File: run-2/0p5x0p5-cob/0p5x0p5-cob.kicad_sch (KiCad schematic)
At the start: 6 parts

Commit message: updating libs for 76 pin
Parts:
- U102: footprint WaferSpace:waferspace_p5xp5_padring -> WaferSpace:waferspace_p5xp5_padring_staggered
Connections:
- net GND: now also U102.58 (MP)
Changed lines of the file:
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@@
+	(wire
+		(pts
+			(xy 215.9 99.06) (xy 215.9 105.41)
+		)
+		(stroke
+			(width 0)
+			(type default)
+		)
+	)
 	(wire
 		(pts
@@
 				(path "/f44d2c8c-cc6e-4ce2-9d41-a48405cdfa9d"
 					(reference "#PWR030")
+					(unit 1)
+				)
+			)
+		)
+	)
+	(symbol
+		(lib_id "power:GND")
+		(at 215.9 105.41 0)
+		(unit 1)
+		(body_style 1)
+		(exclude_from_sim no)
+		(in_bom yes)
+		(on_board yes)
+		(in_pos_files yes)
+		(dnp no)
+		(fields_autoplaced yes)
+		(property "Reference" "#PWR010"
+			(at 215.9 111.76 0)
+			(hide yes)
+			(show_name no)
+			(do_not_autoplace no)
+			(effects
+				(font
+					(size 1.27 1.27)
+				)
+			)
+		)
+		(property "Value" "GND"
+			(at 215.9 110.49 0)
+			(show_name no)
+			(do_not_autoplace no)
+			(effects
+				(font
+					(size 1.27 1.27)
+				)
+			)
+		)
+		(property "Footprint" ""
+			(at 215.9 105.41 0)
+			(hide yes)
+			(show_name no)
+			(do_not_autoplace no)
+			(effects
+				(font
+					(size 1.27 1.27)
+				)
+			)
+		)
+		(property "Datasheet" ""
+			(at 215.9 105.41 0)
+			(hide yes)
+			(show_name no)
+			(do_not_autoplace no)
+			(effects
+				(font
+					(size 1.27 1.27)
+				)
+			)
+		)
+		(property "Description" "Power symbol creates a global label with name \"GND\" , ground"
+			(at 215.9 105.41 0)
+			(hide yes)
+			(show_name no)
+			(do_not_autoplace no)
+			(effects
+				(font
+					(size 1.27 1.27)
+				)
+			)
+		)
+		(pin "1"
+		)
+		(instances
+			(project "0p5x0p5-cob"
+				(path "/f44d2c8c-cc6e-4ce2-9d41-a48405cdfa9d"
+					(reference "#PWR010")
 					(unit 1)
 				)
@@
 			)
 		)
-		(property "Footprint" "WaferSpace:waferspace_p5xp5_padring"
+		(property "Footprint" "WaferSpace:waferspace_p5xp5_padring_staggered"
 			(at 179.07 99.06 0)
 			(hide yes)
@@
 		(pin "16"
 		)
+		(pin "58"
+		)
 		(instances

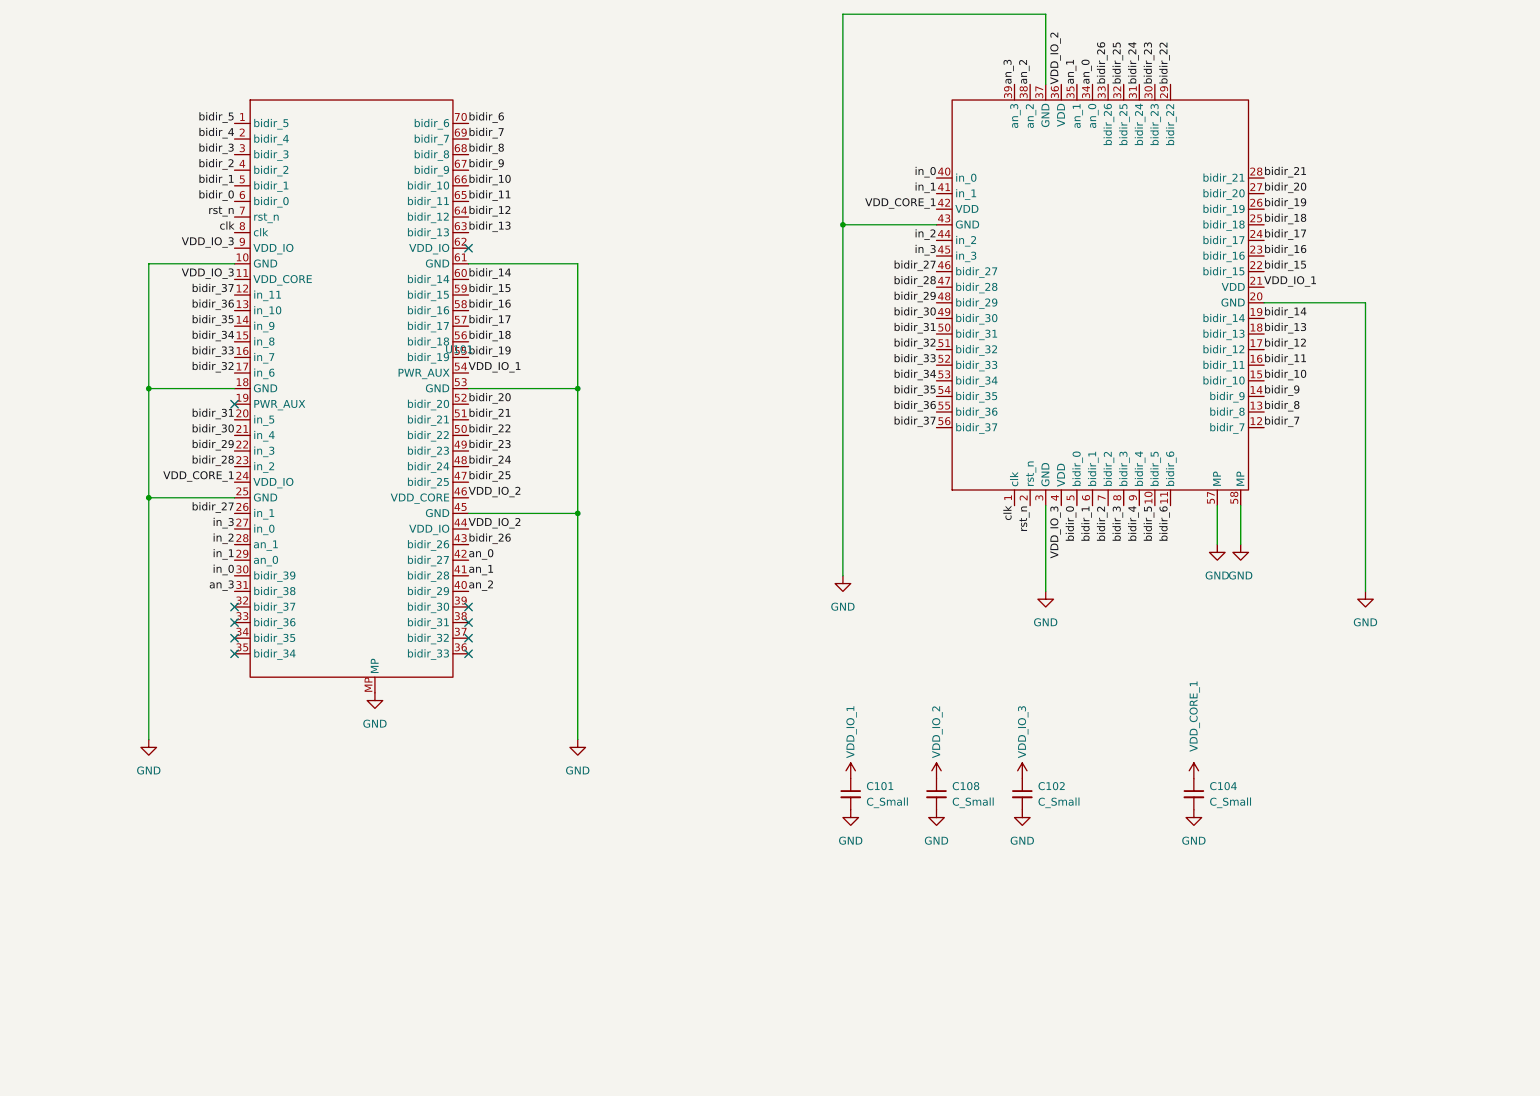
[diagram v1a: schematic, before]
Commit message: finished init routing front only
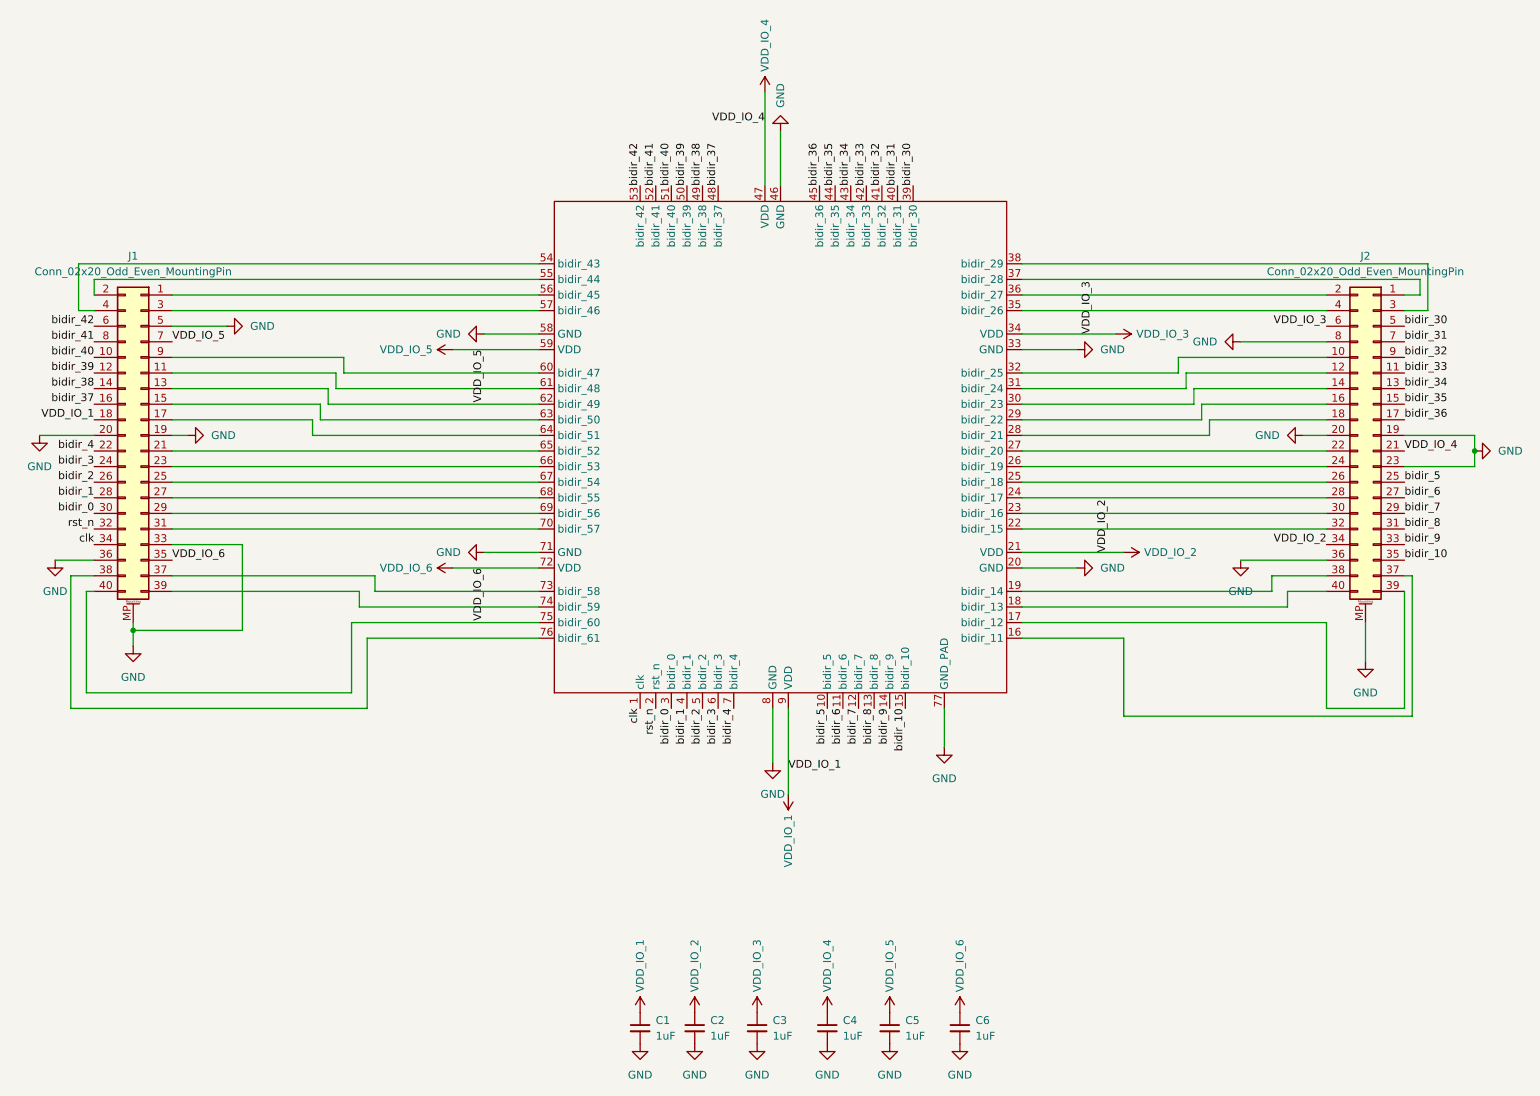
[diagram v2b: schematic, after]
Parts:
- removed C104: C_Small, Capacitor_SMD:C_0201_0603Metric, symbol Device:C_Small
- removed U101: (no value), WaferSpace:CONN-SMD_70P-P0.40_HCTL_HC-PBB40C-70DP-0.4V-02, symbol WaferSpace:70pin_ws_default_mezzanine
- removed U102: (no value), WaferSpace:waferspace_p5xp5_padring_staggered, symbol WaferSpace:0p5x0p5
- added C4, C5, C6: 1uF, Capacitor_SMD:C_0201_0603Metric, symbol Device:C_Small
- added J1, J2: Conn_02x20_Odd_Even_MountingPin, Connector_Hirose_DF40:Hirose_DF40C-40DP-0.4V_2x20-1MP_P0.4mm, symbol Connector_Generic_MountingPin:Conn_02x20_Odd_Even_MountingPin
- added U1: (no value), WaferSpace:0p5x0p5_76, symbol WaferSpace:0p5x0p5_76
- C1: renamed from C101; value C_Small -> 1uF
- C2: renamed from C108; value C_Small -> 1uF
- C3: renamed from C102; value C_Small -> 1uF
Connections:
- net GND: now also C4.2, C5.2, C6.2, J1.19 (Pin_19), J1.20 (Pin_20), J1.33 (Pin_33), J1.36 (Pin_36), J1.5 (Pin_5), J1.MP (MountPin), J2.19 (Pin_19), J2.20 (Pin_20), J2.23 (Pin_23), J2.36 (Pin_36), J2.8 (Pin_8), J2.MP (MountPin), U1.20 (GND), U1.33 (GND), U1.46 (GND), U1.58 (GND), U1.71 (GND), U1.77 (GND_PAD), U1.8 (GND)
- net VDD_IO_1: now also J1.18 (Pin_18), U1.9 (VDD)
- net VDD_IO_2: now also J2.34 (Pin_34), U1.21 (VDD)
- net VDD_IO_3: now also J2.6 (Pin_6), U1.34 (VDD)
- net bidir_0: now also J1.30 (Pin_30), U1.3 (bidir_0)
- net bidir_1: now also J1.28 (Pin_28), U1.4 (bidir_1)
- net bidir_10: now also J2.35 (Pin_35), U1.15 (bidir_10)
- net bidir_2: now also J1.26 (Pin_26), U1.5 (bidir_2)
- net bidir_3: now also J1.24 (Pin_24), U1.6 (bidir_3)
- net bidir_30: now also J2.5 (Pin_5), U1.39 (bidir_30)
- net bidir_31: now also J2.7 (Pin_7), U1.40 (bidir_31)
- net bidir_32: now also J2.9 (Pin_9), U1.41 (bidir_32)
- net bidir_33: now also J2.11 (Pin_11), U1.42 (bidir_33)
- net bidir_34: now also J2.13 (Pin_13), U1.43 (bidir_34)
- net bidir_35: now also J2.15 (Pin_15), U1.44 (bidir_35)
- net bidir_36: now also J2.17 (Pin_17), U1.45 (bidir_36)
- net bidir_37: now also J1.16 (Pin_16), U1.48 (bidir_37)
- net bidir_4: now also J1.22 (Pin_22), U1.7 (bidir_4)
- net bidir_5: now also J2.25 (Pin_25), U1.10 (bidir_5)
- net bidir_6: now also J2.27 (Pin_27), U1.11 (bidir_6)
- net bidir_7: now also J2.29 (Pin_29), U1.12 (bidir_7)
- net bidir_8: now also J2.31 (Pin_31), U1.13 (bidir_8)
- net bidir_9: now also J2.33 (Pin_33), U1.14 (bidir_9)
- net clk: now also J1.34 (Pin_34), U1.1 (clk)
- net rst_n: now also J1.32 (Pin_32), U1.2 (rst_n)
- new net: J2.1 (Pin_1), U1.37 (bidir_28)
- new net: J2.10 (Pin_10), U1.32 (bidir_25)
- new net: J2.12 (Pin_12), U1.31 (bidir_24)
- new net: J2.14 (Pin_14), U1.30 (bidir_23)
- new net: J2.16 (Pin_16), U1.29 (bidir_22)
- new net: J2.18 (Pin_18), U1.28 (bidir_21)
- new net: J2.2 (Pin_2), U1.36 (bidir_27)
- new net: J2.22 (Pin_22), U1.27 (bidir_20)
- new net: J2.24 (Pin_24), U1.26 (bidir_19)
- new net: J2.26 (Pin_26), U1.25 (bidir_18)
- new net: J2.28 (Pin_28), U1.24 (bidir_17)
- new net: J2.3 (Pin_3), U1.38 (bidir_29)
- new net: J2.30 (Pin_30), U1.23 (bidir_16)
- new net: J2.32 (Pin_32), U1.22 (bidir_15)
- new net: J2.37 (Pin_37), U1.16 (bidir_11)
- new net: J2.38 (Pin_38), U1.19 (bidir_14)
- new net: J2.39 (Pin_39), U1.17 (bidir_12)
- new net: J2.4 (Pin_4), U1.35 (bidir_26)
- new net: J2.40 (Pin_40), U1.18 (bidir_13)
- new net: J1.1 (Pin_1), U1.56 (bidir_45)
- new net: J1.11 (Pin_11), U1.61 (bidir_48)
- new net: J1.13 (Pin_13), U1.62 (bidir_49)
- new net: J1.15 (Pin_15), U1.63 (bidir_50)
- new net: J1.17 (Pin_17), U1.64 (bidir_51)
- new net: J1.2 (Pin_2), U1.55 (bidir_44)
- new net: J1.21 (Pin_21), U1.65 (bidir_52)
- new net: J1.23 (Pin_23), U1.66 (bidir_53)
- new net: J1.25 (Pin_25), U1.67 (bidir_54)
- new net: J1.27 (Pin_27), U1.68 (bidir_55)
- new net: J1.29 (Pin_29), U1.69 (bidir_56)
- new net: J1.3 (Pin_3), U1.57 (bidir_46)
- new net: J1.31 (Pin_31), U1.70 (bidir_57)
- new net: J1.37 (Pin_37), U1.73 (bidir_58)
- new net: J1.38 (Pin_38), U1.76 (bidir_61)
- new net: J1.39 (Pin_39), U1., U1.74 (bidir_59)
- new net: J1.4 (Pin_4), U1.54 (bidir_43)
- new net: J1.40 (Pin_40), U1.75 (bidir_60)
- new net: J1.9 (Pin_9), U1.60 (bidir_47)
- new net VDD_IO_4: C4.1, J2.21 (Pin_21), U1.47 (VDD)
- new net VDD_IO_5: C5.1, J1.7 (Pin_7), U1.59 (VDD)
- new net VDD_IO_6: C6.1, J1.35 (Pin_35), U1.72 (VDD)
- new net bidir_38: J1.14 (Pin_14), U1.49 (bidir_38)
- new net bidir_39: J1.12 (Pin_12), U1.50 (bidir_39)
- new net bidir_40: J1.10 (Pin_10), U1.51 (bidir_40)
- new net bidir_41: J1.8 (Pin_8), U1.52 (bidir_41)
- new net bidir_42: J1.6 (Pin_6), U1.53 (bidir_42)
- no-connect marks 10 -> 0
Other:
- moved on the sheet: C1, C2, C3

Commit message: designed v1 of 76 pin package
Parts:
- added CAT_1: pusheen_graphics, WaferSpace:pusheen_back, symbol Connector:Conn_01x01_Pin
- U1: footprint WaferSpace:0p5x0p5_76 -> WaferSpace:waferspace_p5xp5_padring_staggered
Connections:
- net GND: now also U1.78 (GND_PAD), U1.79 (GND_PAD), U1.80 (GND_PAD), U1.81 (GND_PAD)
- net at J2.37 (Pin_37): now also U1.17 (bidir_12); no longer U1.16 (bidir_11)
- net at J2.39 (Pin_39): now also U1.16 (bidir_11); no longer U1.17 (bidir_12)
- net at J1.38 (Pin_38): now also U1.75 (bidir_60); no longer U1.76 (bidir_61)
- net at J1.40 (Pin_40): now also U1.76 (bidir_61); no longer U1.75 (bidir_60)
- no-connect marks 0 -> 1
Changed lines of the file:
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@@
 	)
 	(junction
+		(at 172.72 134.62)
+		(diameter 0)
+		(color 0 0 0 0)
+	)
+	(junction
+		(at 170.18 134.62)
+		(diameter 0)
+		(color 0 0 0 0)
+	)
+	(junction
+		(at 167.64 134.62)
+		(diameter 0)
+		(color 0 0 0 0)
+	)
+	(junction
 		(at 254 90.17)
 		(diameter 0)
 		(color 0 0 0 0)
 	)
+	(junction
+		(at 175.26 134.62)
+		(diameter 0)
+		(color 0 0 0 0)
+	)
+	(no_connect
+		(at 49.53 176.53)
+	)
 	(wire
 		(pts
@@
 	(wire
 		(pts
-			(xy 27.94 129.54) (xy 71.12 129.54)
+			(xy 69.85 77.47) (xy 101.6 77.47)
 		)
 		(stroke
@@
 	(wire
 		(pts
-			(xy 69.85 77.47) (xy 101.6 77.47)
+			(xy 139.7 132.08) (xy 139.7 140.97)
 		)
 		(stroke
@@
 	(wire
 		(pts
-			(xy 139.7 132.08) (xy 139.7 140.97)
+			(xy 180.34 95.25) (xy 229.87 95.25)
 		)
 		(stroke
@@
 	(wire
 		(pts
-			(xy 180.34 95.25) (xy 229.87 95.25)
+			(xy 180.34 71.12) (xy 195.58 71.12)
 		)
 		(stroke
@@
 	(wire
 		(pts
-			(xy 180.34 71.12) (xy 195.58 71.12)
+			(xy 207.01 80.01) (xy 207.01 77.47)
 		)
 		(stroke
@@
 	(wire
 		(pts
-			(xy 207.01 80.01) (xy 207.01 77.47)
+			(xy 41.91 92.71) (xy 101.6 92.71)
 		)
 		(stroke
@@
 	(wire
 		(pts
-			(xy 41.91 92.71) (xy 101.6 92.71)
+			(xy 229.87 132.08) (xy 247.65 132.08)
 		)
 		(stroke
@@
 	(wire
 		(pts
+			(xy 27.94 132.08) (xy 73.66 132.08)
+		)
+		(stroke
+			(width 0)
+			(type default)
+		)
+	)
+	(wire
+		(pts
 			(xy 207.01 77.47) (xy 229.87 77.47)
 		)
@@
 	(wire
 		(pts
+			(xy 177.8 134.62) (xy 175.26 134.62)
+		)
+		(stroke
+			(width 0)
+			(type default)
+		)
+	)
+	(wire
+		(pts
 			(xy 41.91 85.09) (xy 64.77 85.09)
 		)
@@
 	(wire
 		(pts
+			(xy 242.57 133.35) (xy 196.85 133.35)
+		)
+		(stroke
+			(width 0)
+			(type default)
+		)
+	)
+	(wire
+		(pts
 			(xy 67.31 80.01) (xy 67.31 82.55)
 		)
@@
 	(wire
 		(pts
+			(xy 177.8 132.08) (xy 177.8 134.62)
+		)
+		(stroke
+			(width 0)
+			(type default)
+		)
+	)
+	(wire
+		(pts
 			(xy 68.58 80.01) (xy 101.6 80.01)
 		)
@@
 	(wire
 		(pts
-			(xy 243.84 110.49) (xy 243.84 133.35)
+			(xy 175.26 132.08) (xy 175.26 134.62)
 		)
 		(stroke
@@
 	(wire
 		(pts
-			(xy 243.84 133.35) (xy 196.85 133.35)
+			(xy 210.82 87.63) (xy 210.82 85.09)
 		)
 		(stroke
@@
 	(wire
 		(pts
-			(xy 210.82 87.63) (xy 210.82 85.09)
+			(xy 41.91 95.25) (xy 101.6 95.25)
 		)
 		(stroke
@@
 	(wire
 		(pts
-			(xy 41.91 95.25) (xy 101.6 95.25)
+			(xy 246.38 59.69) (xy 246.38 67.31)
 		)
 		(stroke
@@
 	(wire
 		(pts
-			(xy 246.38 59.69) (xy 246.38 67.31)
+			(xy 25.4 129.54) (xy 71.12 129.54)
 		)
 		(stroke
@@
 	(wire
 		(pts
+			(xy 167.64 134.62) (xy 170.18 134.62)
+		)
+		(stroke
+			(width 0)
+			(type default)
+		)
+	)
+	(wire
+		(pts
 			(xy 41.91 113.03) (xy 72.39 113.03)
 		)
@@
 	(wire
 		(pts
-			(xy 167.64 132.08) (xy 167.64 138.43)
+			(xy 167.64 132.08) (xy 167.64 134.62)
 		)
 		(stroke
@@
 	(wire
 		(pts
-			(xy 242.57 132.08) (xy 242.57 113.03)
+			(xy 41.91 82.55) (xy 66.04 82.55)
 		)
 		(stroke
@@
 	(wire
 		(pts
-			(xy 41.91 82.55) (xy 66.04 82.55)
+			(xy 175.26 134.62) (xy 172.72 134.62)
 		)
 		(stroke
@@
 	(wire
 		(pts
-			(xy 27.94 113.03) (xy 27.94 129.54)
-		)
-		(stroke
-			(width 0)
-			(type default)
-		)
-	)
-	(wire
-		(pts
 			(xy 87.63 109.22) (xy 101.6 109.22)
 		)
@@
 	(wire
 		(pts
-			(xy 25.4 132.08) (xy 73.66 132.08)
+			(xy 138.43 31.75) (xy 138.43 46.99)
 		)
 		(stroke
@@
 	(wire
 		(pts
-			(xy 138.43 31.75) (xy 138.43 46.99)
+			(xy 41.91 80.01) (xy 67.31 80.01)
 		)
 		(stroke
@@
 	(wire
 		(pts
-			(xy 41.91 80.01) (xy 67.31 80.01)
+			(xy 69.85 74.93) (xy 69.85 77.47)
 		)
 		(stroke
@@
 	(wire
 		(pts
-			(xy 69.85 74.93) (xy 69.85 77.47)
+			(xy 170.18 132.08) (xy 170.18 134.62)
 		)
 		(stroke
@@
 	(wire
 		(pts
-			(xy 242.57 110.49) (xy 243.84 110.49)
+			(xy 242.57 110.49) (xy 247.65 110.49)
 		)
 		(stroke
@@
 	(wire
 		(pts
+			(xy 172.72 132.08) (xy 172.72 134.62)
+		)
+		(stroke
+			(width 0)
+			(type default)
+		)
+	)
+	(wire
+		(pts
 			(xy 245.11 62.23) (xy 245.11 64.77)
 		)
@@
 	(wire
 		(pts
+			(xy 167.64 134.62) (xy 167.64 138.43)
+		)
+		(stroke
+			(width 0)
+			(type default)
+		)
+	)
+	(wire
+		(pts
 			(xy 29.21 62.23) (xy 101.6 62.23)
 		)
@@
 	(wire
 		(pts
+			(xy 25.4 110.49) (xy 25.4 129.54)
+		)
+		(stroke
+			(width 0)
+			(type default)
+		)
+	)
+	(wire
+		(pts
 			(xy 246.38 67.31) (xy 242.57 67.31)
 		)
@@
 	(wire
 		(pts
+			(xy 170.18 134.62) (xy 172.72 134.62)
+		)
+		(stroke
+			(width 0)
+			(type default)
+		)
+	)
+	(wire
+		(pts
+			(xy 247.65 132.08) (xy 247.65 110.49)
+		)
+		(stroke
+			(width 0)
+			(type default)
+		)
+	)
+	(wire
+		(pts
 			(xy 180.34 102.87) (xy 229.87 102.87)
 		)
@@
 	(wire
 		(pts
-			(xy 25.4 110.49) (xy 25.4 132.08)
+			(xy 223.52 113.03) (xy 223.52 115.57)
 		)
 		(stroke
@@
 	(wire
 		(pts
-			(xy 223.52 113.03) (xy 223.52 115.57)
+			(xy 27.94 113.03) (xy 27.94 132.08)
 		)
 		(stroke
@@
 	(wire
 		(pts
-			(xy 229.87 132.08) (xy 242.57 132.08)
+			(xy 180.34 82.55) (xy 208.28 82.55)
 		)
 		(stroke
@@
 	(wire
 		(pts
-			(xy 180.34 82.55) (xy 208.28 82.55)
+			(xy 242.57 113.03) (xy 242.57 133.35)
 		)
 		(stroke
@@
 			)
 		)
-		(property "Footprint" "WaferSpace:0p5x0p5_76"
+		(property "Footprint" "WaferSpace:waferspace_p5xp5_padring_staggered"
 			(at 141.732 94.488 0)
 			(hide yes)
@@
 		(pin "77"
 		)
+		(pin "80"
+		)
+		(pin "78"
+		)
+		(pin "79"
+		)
+		(pin "81"
+		)
 		(instances
 			(project "0p5x0p5-cob"
@@
 					(unit 1)
 				)
+			)
+		)
+	)
+	(symbol
+		(lib_id "Connector:Conn_01x01_Pin")
+		(at 44.45 176.53 0)
+		(unit 1)
+		(body_style 1)
+		(exclude_from_sim no)
+		(in_bom yes)
+		(on_board yes)
+		(in_pos_files yes)
+		(dnp no)
+		(fields_autoplaced yes)
+		(property "Reference" "CAT_1"
+			(at 45.085 171.45 0)
+			(show_name no)
+			(do_not_autoplace no)
+			(effects
+				(font
+					(size 1.27 1.27)
+				)
+			)
+		)
+		(property "Value" "pusheen_graphics"
+			(at 45.085 173.99 0)
+			(show_name no)
+			(do_not_autoplace no)
+			(effects
+				(font
+					(size 1.27 1.27)
+				)
+			)
+		)
+		(property "Footprint" "WaferSpace:pusheen_back"
+			(at 44.45 176.53 0)
+			(hide yes)
+			(show_name no)
+			(do_not_autoplace no)
+			(effects
+				(font
+					(size 1.27 1.27)
+				)
+			)
+		)
+		(property "Datasheet" ""
+			(at 44.45 176.53 0)
+			(hide yes)
+			(show_name no)
+			(do_not_autoplace no)
+			(effects
+				(font
+					(size 1.27 1.27)
+				)
+			)
+		)
+		(property "Description" "Generic connector, single row, 01x01, script generated"
+			(at 44.45 176.53 0)
+			(hide yes)
+			(show_name no)
+			(do_not_autoplace no)
+			(effects
+				(font
+					(size 1.27 1.27)
+				)
+			)
+		)
+		(pin "1"
+		)
+		(instances
+			(project "0p5x0p5-cob"
+				(path "/f44d2c8c-cc6e-4ce2-9d41-a48405cdfa9d"
+					(reference "CAT_1")
+					(unit 1)
+				)
